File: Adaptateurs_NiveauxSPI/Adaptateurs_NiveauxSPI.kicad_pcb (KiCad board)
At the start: 2 copper layers, 21 parts, among them P1 CONN_01X07, P2 CONN_01X08, P3 CONN_01X07, P4 CONN_01X12, P5 CONN_01X07, P6 CONN_01X09, P7 CONN_01X07, P8 CONN_01X10, U1 CON_5V_3-3V, U2 CON_5V_3-3V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

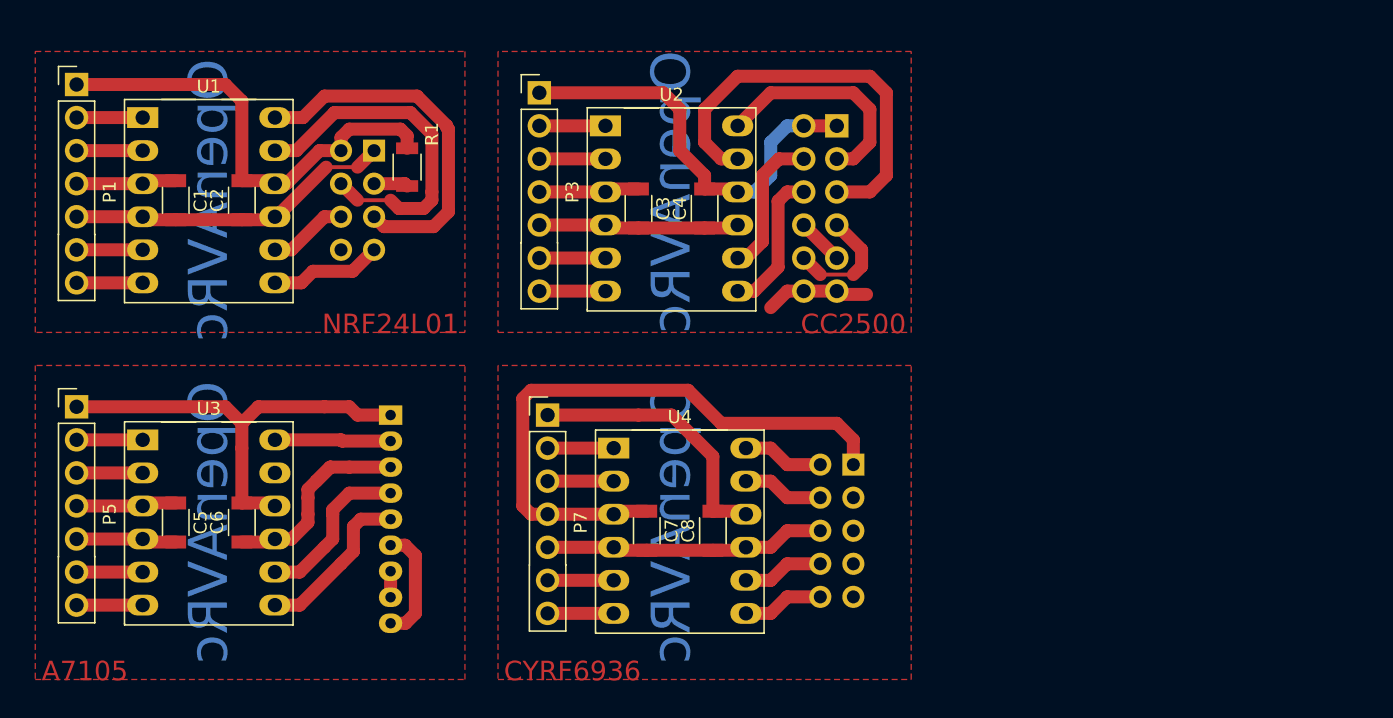
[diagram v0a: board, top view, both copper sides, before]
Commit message: Update projet
- Add RFM95W
- Add MPM 4in1
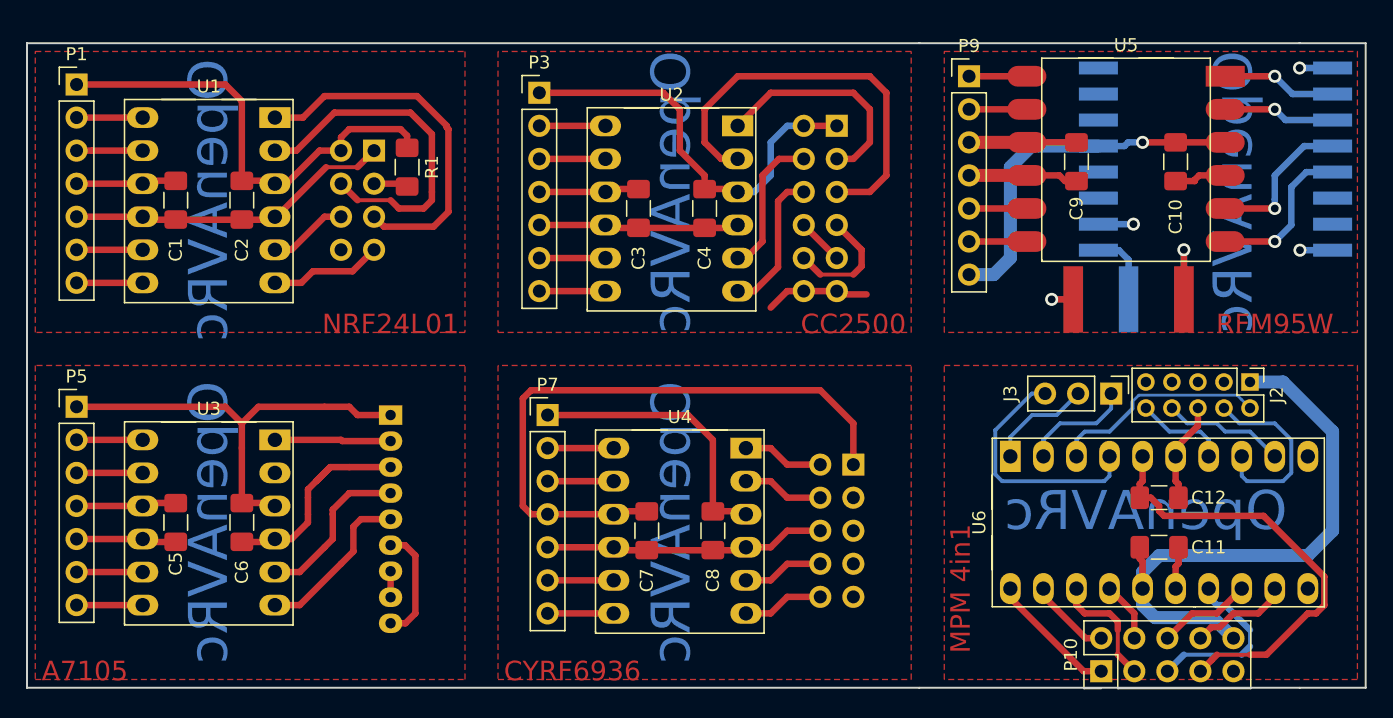
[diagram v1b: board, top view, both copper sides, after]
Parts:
- added C10: 100nF, Capacitor_SMD:C_1206_3216Metric_Pad1.42x1.75mm_HandSolder, F.Cu at (196.2, 72.6)
- added C11: 100nF, Capacitor_SMD:C_1206_3216Metric_Pad1.42x1.75mm_HandSolder, F.Cu at (194.9, 102.2)
- added C12: 100nF, Capacitor_SMD:C_1206_3216Metric_Pad1.42x1.75mm_HandSolder, F.Cu at (194.9, 98.4)
- added C9: 100nF, Capacitor_SMD:C_1206_3216Metric_Pad1.42x1.75mm_HandSolder, F.Cu at (188.6, 72.6)
- added J1: RFM95W, Conv_SPI:RFM95W, B.Cu at (199.3, 72.4)
- added J2: MPM_ 4en1, Connector_PinHeader_2.00mm:PinHeader_2x05_P2.00mm_Vertical, F.Cu at (201.9, 89.5)
- added J3: MPM_4in1, Connector_PinHeader_2.54mm:PinHeader_1x03_P2.54mm_Vertical, F.Cu at (191.3, 90.4)
- added J4: SMA, Conv_SPI:SMA_Amphenol_132289_EdgeMount, B.Cu at (192.6, 83.2)
- added P10: SpirfMod, Connector_PinHeader_2.54mm:PinHeader_2x05_P2.54mm_Vertical, F.Cu at (190.5, 111.8)
- added P9: SpirfMod, Connector_PinHeader_2.54mm:PinHeader_1x07_P2.54mm_Vertical, F.Cu at (180.3, 66.0)
- added U5: CONV_5V/3.3V, Conv_SPI:Level_Convertissor_SMD, F.Cu at (187.3, 66.0)
- added U6: CONV_5V_3-3V_8, Conv_SPI:Level_Convertissor_8_W10.16mm, F.Cu at (183.5, 105.4)
- C1, C2, C3, C4, C5, C6, C7, C8: footprint C_1206 -> Capacitor_SMD:C_1206_3216Metric_Pad1.42x1.75mm_HandSolder
- P1: value CONN_01X07 -> SpirfMod; footprint Pin_Header_Straight_1x07_Pitch2.54mm -> Connector_PinHeader_2.54mm:PinHeader_1x07_P2.54mm_Vertical
- P2: value CONN_01X08 -> NRF24L01; footprint Pin_Header_Straight_2x04_Pitch2.54mm -> Connector_PinHeader_2.54mm:PinHeader_2x04_P2.54mm_Vertical
- P3: value CONN_01X07 -> SpirfMod; footprint Shield_Lib:Pin_Header_Straight_1x05_Pitch2.54mm -> Connector_PinHeader_2.54mm:PinHeader_1x07_P2.54mm_Vertical
- P4: value CONN_01X12 -> CC2500; footprint Shield_Lib:Pin_Header_Straight_2x05_Pitch2.54mm -> Connector_PinHeader_2.54mm:PinHeader_2x06_P2.54mm_Vertical
- P5: value CONN_01X07 -> SpirMod; footprint Pin_Header_Straight_1x07_Pitch2.54mm -> Connector_PinHeader_2.54mm:PinHeader_1x07_P2.54mm_Vertical
- P6: value CONN_01X09 -> A7105; footprint Pin_Header_Straight_1x09_Pitch2.54mm -> Conv_SPI:Pin_Header_Straight_1x09_Pitch2mm
- P7: footprint Pin_Header_Straight_1x07_Pitch2.54mm -> Connector_PinHeader_2.54mm:PinHeader_1x07_P2.54mm_Vertical
- P8: footprint Shield_Lib:Pin_Header_Straight_2x05_Pitch2.54mm -> Connector_PinHeader_2.54mm:PinHeader_2x05_P2.54mm_Vertical
- R1: footprint R_1206 -> Resistor_SMD:R_1206_3216Metric_Pad1.42x1.75mm_HandSolder
- U1, U2, U3, U4: value CON_5V_3-3V -> CONV_5V/3.3V
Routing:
- net +5F: track 0.00 -> 45.3 mm
- net +3V3: track 0.00 -> 34.0 mm
- net GNDS: track 0.00 -> 31.2 mm, vias 0 -> 5
- net +3.3VA: track 0.00 -> 28.0 mm, vias 0 -> 1
- net /A7105: track 0.00 -> 19.1 mm
- net /CYRF: track 0.00 -> 16.8 mm
- net /SCK_L: track 0.00 -> 14.5 mm
- net /MISO: track 0.00 -> 13.3 mm
- net Net-(J1-Pad13): track 0.00 -> 12.2 mm, vias 0 -> 1
- net Net-(J1-Pad12): track 0.00 -> 11.7 mm, vias 0 -> 1
- net GNDREF: track 0.00 -> 11.1 mm
- net /CS-CC2500: track 0.00 -> 10.0 mm
- net /MOSI_L: track 0.00 -> 9.44 mm
- net /CS_CYRF: track 0.00 -> 9.31 mm
- net Net-(J1-Pad10): track 0.00 -> 8.82 mm, vias 0 -> 1
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- added copper zone on F.Cu, net GNDREF
- added copper zone on F.Cu, net GNDS
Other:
- board outline added: 102.9 x 49.5 mm
- net class ALIM added: clearance 0.21, trace_width 1, via_dia 1, via_drill 0.6
- net class Default: clearance 0.2 -> 0.21; trace_width 1 -> 0.5; via_dia 0.6 -> 1; via_drill 0.4 -> 0.6
- rule trace_clearance: 0.2 -> 0.21
- rule trace_min: 0.3 -> 0.21
- rule via_min_size: 0.4 -> 1
- board text added: "MPM 4in1"
- board text added: "RFM95W"
